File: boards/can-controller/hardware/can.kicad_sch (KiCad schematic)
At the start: 55 parts, among them J11 CAN1, J12 CAN2, J13 CAN3, J14 CAN4, U10 ISOW1044, U11 ISOW1044, U12 ISOW1044, U13 ISOW1044

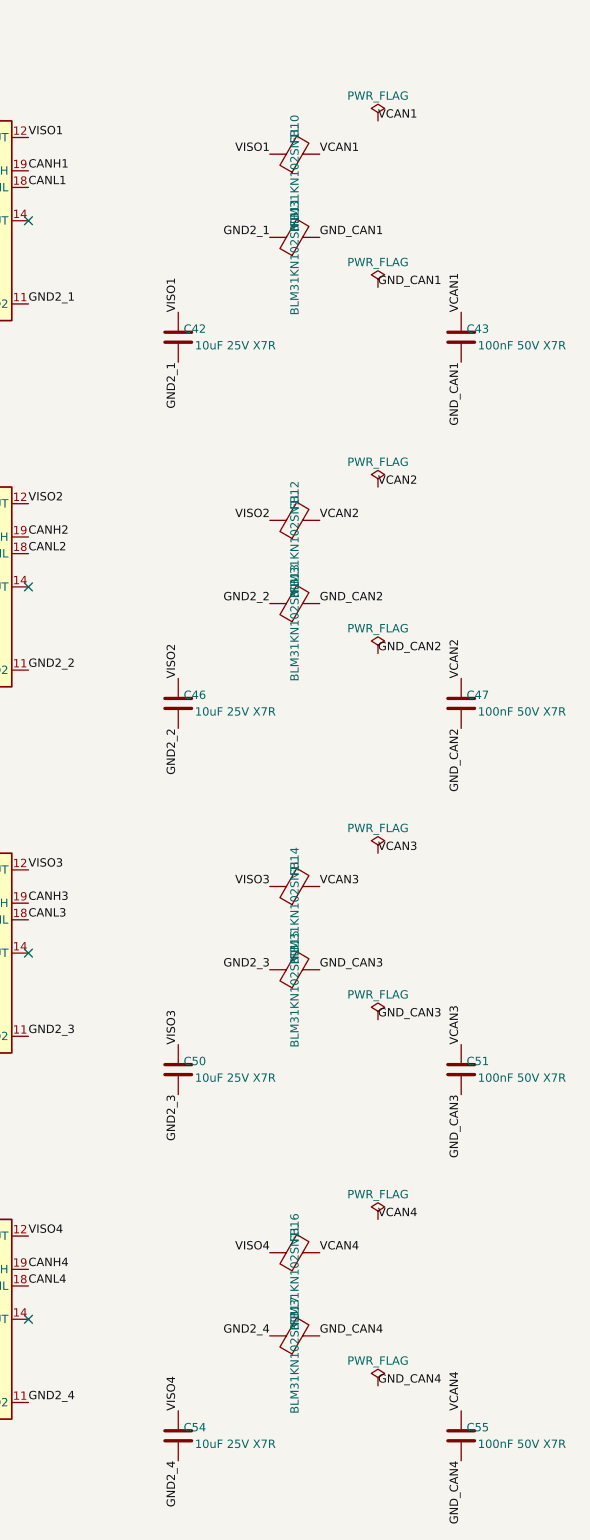
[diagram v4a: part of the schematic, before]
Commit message: Move core, can-card, io-card, serial-card, can-ssr, probe-helper to rev B
Rev A went to PCBWay and is tagged revA. Rev B replaces parts the Mouser
BOM check flagged (obsolete, end of life, not recommended for new designs,
or not orderable) and swaps out-of-stock passives and diodes for in-stock
equivalents. Field-only changes, same footprints, no layout change; the
reference boards (can-controller, pic-module) get the same part numbers.
The rev A order lists (DigiKey, Mouser) carry the same substitutions; the
Mouser list leaves out the T821 box headers (bought from DigiKey).

docs/rev-b-changes.md lists every change and the rev B to-dos (MAX7219 is
obsolete and must be replaced). transfer/mouser-revA.xlsx (Mouser BOM
check) consumed.

Co-Authored-By: Claude Opus 5.5 <noreply@anthropic.com>
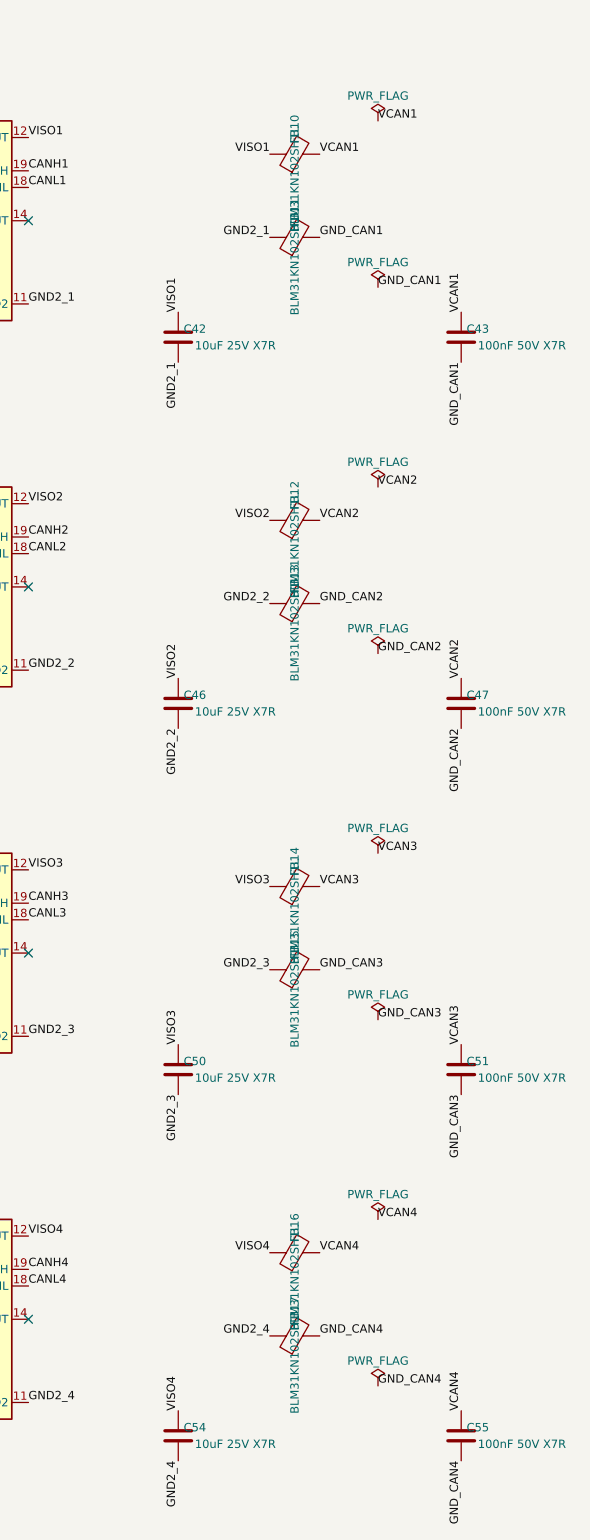
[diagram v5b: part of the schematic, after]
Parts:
- C40, C43, C44, C47, C48, C51, C52, C55: MPN GRM21BR71H104KA01L -> C0805C104K5RACTU; Manufacturer Murata -> KEMET
- C41, C42, C45, C46, C49, C50, C53, C54: MPN GRM31CR71E106KA12L -> CL31B106KAHNNNE; Manufacturer Murata -> Samsung Electro-Mechanics
- FB10, FB11, FB12, FB13, FB14, FB15, FB16, FB17: value BLM31KN102SN1L -> BLM31KN102SH1L; MPN BLM31KN102SN1L -> BLM31KN102SH1L
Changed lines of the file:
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@@
 			)
 		)
-		(property "Manufacturer" "Murata"
+		(property "Manufacturer" "KEMET"
 			(at 63.5 81.28 0)
 			(hide yes)
@@
 			)
 		)
-		(property "MPN" "GRM21BR71H104KA01L"
+		(property "MPN" "C0805C104K5RACTU"
 			(at 63.5 81.28 0)
 			(hide yes)
@@
 			)
 		)
-		(property "Manufacturer" "Murata"
+		(property "Manufacturer" "Samsung Electro-Mechanics"
 			(at 76.2 81.28 0)
 			(hide yes)
@@
 			)
 		)
-		(property "MPN" "GRM31CR71E106KA12L"
+		(property "MPN" "CL31B106KAHNNNE"
 			(at 76.2 81.28 0)
 			(hide yes)
@@
 			)
 		)
-		(property "Manufacturer" "Murata"
+		(property "Manufacturer" "Samsung Electro-Mechanics"
 			(at 149.86 81.28 0)
 			(hide yes)
@@
 			)
 		)
-		(property "MPN" "GRM31CR71E106KA12L"
+		(property "MPN" "CL31B106KAHNNNE"
 			(at 149.86 81.28 0)
 			(hide yes)
@@
 			)
 		)
-		(property "Manufacturer" "Murata"
+		(property "Manufacturer" "KEMET"
 			(at 193.04 81.28 0)
 			(hide yes)
@@
 			)
 		)
-		(property "MPN" "GRM21BR71H104KA01L"
+		(property "MPN" "C0805C104K5RACTU"
 			(at 193.04 81.28 0)
 			(hide yes)
@@
 			)
 		)
-		(property "Value" "BLM31KN102SN1L"
+		(property "Value" "BLM31KN102SH1L"
 			(at 167.64 57.15 0)
 			(effects
@@
 			)
 		)
-		(property "MPN" "BLM31KN102SN1L"
+		(property "MPN" "BLM31KN102SH1L"
 			(at 167.64 53.34 0)
 			(hide yes)
@@
 			)
 		)
-		(property "Value" "BLM31KN102SN1L"
+		(property "Value" "BLM31KN102SH1L"
 			(at 167.64 69.85 0)
 			(effects
@@
 			)
 		)
-		(property "MPN" "BLM31KN102SN1L"
+		(property "MPN" "BLM31KN102SH1L"
 			(at 167.64 66.04 0)
 			(hide yes)
@@
 			)
 		)
-		(property "Manufacturer" "Murata"
+		(property "Manufacturer" "KEMET"
 			(at 63.5 137.16 0)
 			(hide yes)
@@
 			)
 		)
-		(property "MPN" "GRM21BR71H104KA01L"
+		(property "MPN" "C0805C104K5RACTU"
 			(at 63.5 137.16 0)
 			(hide yes)
@@
 			)
 		)
-		(property "Manufacturer" "Murata"
+		(property "Manufacturer" "Samsung Electro-Mechanics"
 			(at 76.2 137.16 0)
 			(hide yes)
@@
 			)
 		)
-		(property "MPN" "GRM31CR71E106KA12L"
+		(property "MPN" "CL31B106KAHNNNE"
 			(at 76.2 137.16 0)
 			(hide yes)
@@
 			)
 		)
-		(property "Manufacturer" "Murata"
+		(property "Manufacturer" "Samsung Electro-Mechanics"
 			(at 149.86 137.16 0)
 			(hide yes)
@@
 			)
 		)
-		(property "MPN" "GRM31CR71E106KA12L"
+		(property "MPN" "CL31B106KAHNNNE"
 			(at 149.86 137.16 0)
 			(hide yes)
@@
 			)
 		)
-		(property "Manufacturer" "Murata"
+		(property "Manufacturer" "KEMET"
 			(at 193.04 137.16 0)
 			(hide yes)
@@
 			)
 		)
-		(property "MPN" "GRM21BR71H104KA01L"
+		(property "MPN" "C0805C104K5RACTU"
 			(at 193.04 137.16 0)
 			(hide yes)
@@
 			)
 		)
-		(property "Value" "BLM31KN102SN1L"
+		(property "Value" "BLM31KN102SH1L"
 			(at 167.64 113.03 0)
 			(effects
@@
 			)
 		)
-		(property "MPN" "BLM31KN102SN1L"
+		(property "MPN" "BLM31KN102SH1L"
 			(at 167.64 109.22 0)
 			(hide yes)
@@
 			)
 		)
-		(property "Value" "BLM31KN102SN1L"
+		(property "Value" "BLM31KN102SH1L"
 			(at 167.64 125.73 0)
 			(effects
@@
 			)
 		)
-		(property "MPN" "BLM31KN102SN1L"
+		(property "MPN" "BLM31KN102SH1L"
 			(at 167.64 121.92 0)
 			(hide yes)
@@
 			)
 		)
-		(property "Manufacturer" "Murata"
+		(property "Manufacturer" "KEMET"
 			(at 63.5 193.04 0)
 			(hide yes)
@@
 			)
 		)
-		(property "MPN" "GRM21BR71H104KA01L"
+		(property "MPN" "C0805C104K5RACTU"
 			(at 63.5 193.04 0)
 			(hide yes)
@@
 			)
 		)
-		(property "Manufacturer" "Murata"
+		(property "Manufacturer" "Samsung Electro-Mechanics"
 			(at 76.2 193.04 0)
 			(hide yes)
@@
 			)
 		)
-		(property "MPN" "GRM31CR71E106KA12L"
+		(property "MPN" "CL31B106KAHNNNE"
 			(at 76.2 193.04 0)
 			(hide yes)
@@
 			)
 		)
-		(property "Manufacturer" "Murata"
+		(property "Manufacturer" "Samsung Electro-Mechanics"
 			(at 149.86 193.04 0)
 			(hide yes)
@@
 			)
 		)
-		(property "MPN" "GRM31CR71E106KA12L"
+		(property "MPN" "CL31B106KAHNNNE"
 			(at 149.86 193.04 0)
 			(hide yes)
@@
 			)
 		)
-		(property "Manufacturer" "Murata"
+		(property "Manufacturer" "KEMET"
 			(at 193.04 193.04 0)
 			(hide yes)
@@
 			)
 		)
-		(property "MPN" "GRM21BR71H104KA01L"
+		(property "MPN" "C0805C104K5RACTU"
 			(at 193.04 193.04 0)
 			(hide yes)
@@
 			)
 		)
-		(property "Value" "BLM31KN102SN1L"
+		(property "Value" "BLM31KN102SH1L"
 			(at 167.64 168.91 0)
 			(effects
@@
 			)
 		)
-		(property "MPN" "BLM31KN102SN1L"
+		(property "MPN" "BLM31KN102SH1L"
 			(at 167.64 165.1 0)
 			(hide yes)
@@
 			)
 		)
-		(property "Value" "BLM31KN102SN1L"
+		(property "Value" "BLM31KN102SH1L"
 			(at 167.64 181.61 0)
 			(effects
@@
 			)
 		)
-		(property "MPN" "BLM31KN102SN1L"
+		(property "MPN" "BLM31KN102SH1L"
 			(at 167.64 177.8 0)
 			(hide yes)
@@
 			)
 		)
-		(property "Manufacturer" "Murata"
+		(property "Manufacturer" "KEMET"
 			(at 63.5 248.92 0)
 			(hide yes)
@@
 			)
 		)
-		(property "MPN" "GRM21BR71H104KA01L"
+		(property "MPN" "C0805C104K5RACTU"
 			(at 63.5 248.92 0)
 			(hide yes)
@@
 			)
 		)
-		(property "Manufacturer" "Murata"
+		(property "Manufacturer" "Samsung Electro-Mechanics"
 			(at 76.2 248.92 0)
 			(hide yes)
@@
 			)
 		)
-		(property "MPN" "GRM31CR71E106KA12L"
+		(property "MPN" "CL31B106KAHNNNE"
 			(at 76.2 248.92 0)
 			(hide yes)
@@
 			)
 		)
-		(property "Manufacturer" "Murata"
+		(property "Manufacturer" "Samsung Electro-Mechanics"
 			(at 149.86 248.92 0)
 			(hide yes)
@@
 			)
 		)
-		(property "MPN" "GRM31CR71E106KA12L"
+		(property "MPN" "CL31B106KAHNNNE"
 			(at 149.86 248.92 0)
 			(hide yes)
@@
 			)
 		)
-		(property "Manufacturer" "Murata"
+		(property "Manufacturer" "KEMET"
 			(at 193.04 248.92 0)
 			(hide yes)
@@
 			)
 		)
-		(property "MPN" "GRM21BR71H104KA01L"
+		(property "MPN" "C0805C104K5RACTU"
 			(at 193.04 248.92 0)
 			(hide yes)
@@
 			)
 		)
-		(property "Value" "BLM31KN102SN1L"
+		(property "Value" "BLM31KN102SH1L"
 			(at 167.64 224.79 0)
 			(effects
@@
 			)
 		)
-		(property "MPN" "BLM31KN102SN1L"
+		(property "MPN" "BLM31KN102SH1L"
 			(at 167.64 220.98 0)
 			(hide yes)
@@
 			)
 		)
-		(property "Value" "BLM31KN102SN1L"
+		(property "Value" "BLM31KN102SH1L"
 			(at 167.64 237.49 0)
 			(effects
@@
 			)
 		)
-		(property "MPN" "BLM31KN102SN1L"
+		(property "MPN" "BLM31KN102SH1L"
 			(at 167.64 233.68 0)
 			(hide yes)

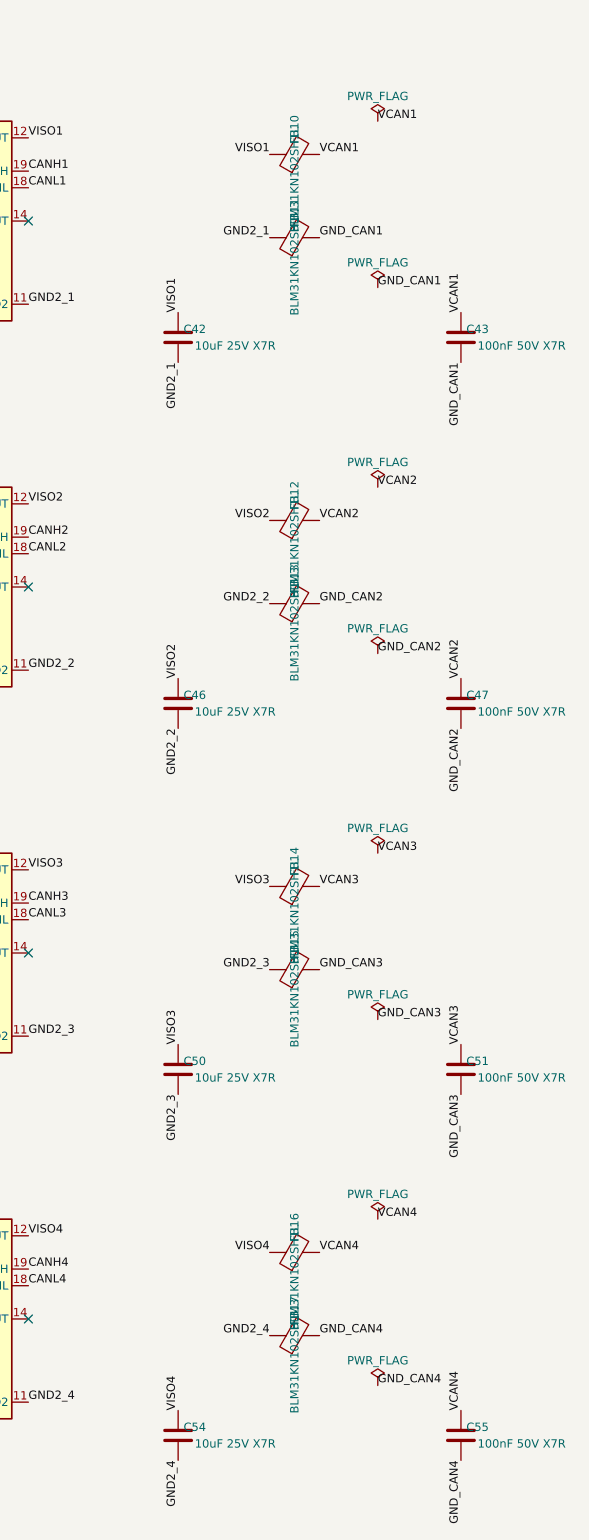
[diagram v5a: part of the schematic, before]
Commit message: Rev B / rev A order: 10 uF CL31B106KAHZW6E, beads BLM31PG391SN1L
Both earlier substitutes (CL31B106KAHNNNE, BLM31KN102SH1L) are on
backorder at Mouser. CL31B106KAHZW6E has the same rating (1.4 mm tall).
The isolated-supply beads need no 1 kOhm: TI's reference uses 330 Ohm;
BLM31PG391SN1L is 390 Ohm @ 100 MHz, 2 A, 50 mOhm. Field-only changes;
order lists regenerated.

Co-Authored-By: Claude Opus 5.5 <noreply@anthropic.com>
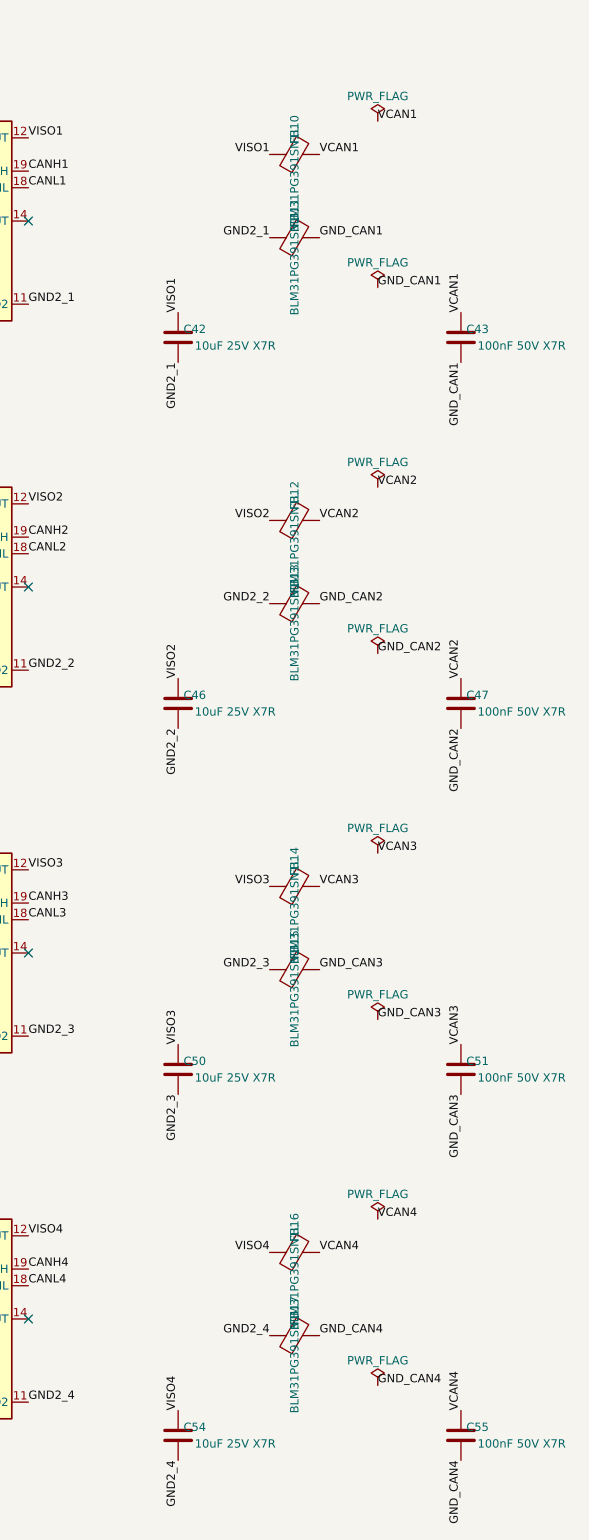
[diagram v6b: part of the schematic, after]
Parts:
- C41, C42, C45, C46, C49, C50, C53, C54: MPN CL31B106KAHNNNE -> CL31B106KAHZW6E
- FB10, FB11, FB12, FB13, FB14, FB15, FB16, FB17: value BLM31KN102SH1L -> BLM31PG391SN1L; MPN BLM31KN102SH1L -> BLM31PG391SN1L
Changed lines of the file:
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@@
 			)
 		)
-		(property "MPN" "CL31B106KAHNNNE"
+		(property "MPN" "CL31B106KAHZW6E"
 			(at 76.2 81.28 0)
 			(hide yes)
@@
 			)
 		)
-		(property "MPN" "CL31B106KAHNNNE"
+		(property "MPN" "CL31B106KAHZW6E"
 			(at 149.86 81.28 0)
 			(hide yes)
@@
 			)
 		)
-		(property "Value" "BLM31KN102SH1L"
+		(property "Value" "BLM31PG391SN1L"
 			(at 167.64 57.15 0)
 			(effects
@@
 			)
 		)
-		(property "MPN" "BLM31KN102SH1L"
+		(property "MPN" "BLM31PG391SN1L"
 			(at 167.64 53.34 0)
 			(hide yes)
@@
 			)
 		)
-		(property "Value" "BLM31KN102SH1L"
+		(property "Value" "BLM31PG391SN1L"
 			(at 167.64 69.85 0)
 			(effects
@@
 			)
 		)
-		(property "MPN" "BLM31KN102SH1L"
+		(property "MPN" "BLM31PG391SN1L"
 			(at 167.64 66.04 0)
 			(hide yes)
@@
 			)
 		)
-		(property "MPN" "CL31B106KAHNNNE"
+		(property "MPN" "CL31B106KAHZW6E"
 			(at 76.2 137.16 0)
 			(hide yes)
@@
 			)
 		)
-		(property "MPN" "CL31B106KAHNNNE"
+		(property "MPN" "CL31B106KAHZW6E"
 			(at 149.86 137.16 0)
 			(hide yes)
@@
 			)
 		)
-		(property "Value" "BLM31KN102SH1L"
+		(property "Value" "BLM31PG391SN1L"
 			(at 167.64 113.03 0)
 			(effects
@@
 			)
 		)
-		(property "MPN" "BLM31KN102SH1L"
+		(property "MPN" "BLM31PG391SN1L"
 			(at 167.64 109.22 0)
 			(hide yes)
@@
 			)
 		)
-		(property "Value" "BLM31KN102SH1L"
+		(property "Value" "BLM31PG391SN1L"
 			(at 167.64 125.73 0)
 			(effects
@@
 			)
 		)
-		(property "MPN" "BLM31KN102SH1L"
+		(property "MPN" "BLM31PG391SN1L"
 			(at 167.64 121.92 0)
 			(hide yes)
@@
 			)
 		)
-		(property "MPN" "CL31B106KAHNNNE"
+		(property "MPN" "CL31B106KAHZW6E"
 			(at 76.2 193.04 0)
 			(hide yes)
@@
 			)
 		)
-		(property "MPN" "CL31B106KAHNNNE"
+		(property "MPN" "CL31B106KAHZW6E"
 			(at 149.86 193.04 0)
 			(hide yes)
@@
 			)
 		)
-		(property "Value" "BLM31KN102SH1L"
+		(property "Value" "BLM31PG391SN1L"
 			(at 167.64 168.91 0)
 			(effects
@@
 			)
 		)
-		(property "MPN" "BLM31KN102SH1L"
+		(property "MPN" "BLM31PG391SN1L"
 			(at 167.64 165.1 0)
 			(hide yes)
@@
 			)
 		)
-		(property "Value" "BLM31KN102SH1L"
+		(property "Value" "BLM31PG391SN1L"
 			(at 167.64 181.61 0)
 			(effects
@@
 			)
 		)
-		(property "MPN" "BLM31KN102SH1L"
+		(property "MPN" "BLM31PG391SN1L"
 			(at 167.64 177.8 0)
 			(hide yes)
@@
 			)
 		)
-		(property "MPN" "CL31B106KAHNNNE"
+		(property "MPN" "CL31B106KAHZW6E"
 			(at 76.2 248.92 0)
 			(hide yes)
@@
 			)
 		)
-		(property "MPN" "CL31B106KAHNNNE"
+		(property "MPN" "CL31B106KAHZW6E"
 			(at 149.86 248.92 0)
 			(hide yes)
@@
 			)
 		)
-		(property "Value" "BLM31KN102SH1L"
+		(property "Value" "BLM31PG391SN1L"
 			(at 167.64 224.79 0)
 			(effects
@@
 			)
 		)
-		(property "MPN" "BLM31KN102SH1L"
+		(property "MPN" "BLM31PG391SN1L"
 			(at 167.64 220.98 0)
 			(hide yes)
@@
 			)
 		)
-		(property "Value" "BLM31KN102SH1L"
+		(property "Value" "BLM31PG391SN1L"
 			(at 167.64 237.49 0)
 			(effects
@@
 			)
 		)
-		(property "MPN" "BLM31KN102SH1L"
+		(property "MPN" "BLM31PG391SN1L"
 			(at 167.64 233.68 0)
 			(hide yes)

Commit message: Rev B / rev A order: ISOW1044BDFMR (ISOW1044DFMR out of stock)
Same TI part, package and pinout with basic instead of reinforced
isolation; the CAN buses are low-voltage and isolated against ground
loops, not for safety. Field-only change on can-card (and the reference
can-controller); order lists regenerated.

Co-Authored-By: Claude Opus 5.5 <noreply@anthropic.com>
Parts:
- U10, U11, U12, U13: value ISOW1044 -> ISOW1044B; MPN ISOW1044DFMR -> ISOW1044BDFMR
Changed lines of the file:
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@@
 			)
 		)
-		(property "Value" "ISOW1044"
+		(property "Value" "ISOW1044B"
 			(at 116.84 83.82 0)
 			(effects
@@
 			)
 		)
-		(property "MPN" "ISOW1044DFMR"
+		(property "MPN" "ISOW1044BDFMR"
 			(at 111.76 63.5 0)
 			(hide yes)
@@
 			)
 		)
-		(property "Value" "ISOW1044"
+		(property "Value" "ISOW1044B"
 			(at 116.84 139.7 0)
 			(effects
@@
 			)
 		)
-		(property "MPN" "ISOW1044DFMR"
+		(property "MPN" "ISOW1044BDFMR"
 			(at 111.76 119.38 0)
 			(hide yes)
@@
 			)
 		)
-		(property "Value" "ISOW1044"
+		(property "Value" "ISOW1044B"
 			(at 116.84 195.58 0)
 			(effects
@@
 			)
 		)
-		(property "MPN" "ISOW1044DFMR"
+		(property "MPN" "ISOW1044BDFMR"
 			(at 111.76 175.26 0)
 			(hide yes)
@@
 			)
 		)
-		(property "Value" "ISOW1044"
+		(property "Value" "ISOW1044B"
 			(at 116.84 251.46 0)
 			(effects
@@
 			)
 		)
-		(property "MPN" "ISOW1044DFMR"
+		(property "MPN" "ISOW1044BDFMR"
 			(at 111.76 231.14 0)
 			(hide yes)
